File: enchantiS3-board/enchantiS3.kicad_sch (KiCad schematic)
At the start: 71 parts, among them J1 USB_C_Receptacle_USB2.0, Q1 BSS138, Q2 BSS138, Q3 BSS138, SW1 B3U-1000P, SW2 B3U-1000P, U1 USBLC6-2P6, U2 MCP73871, U3 NCP167AMX330TBG, U4 NCP167AMX180TBG

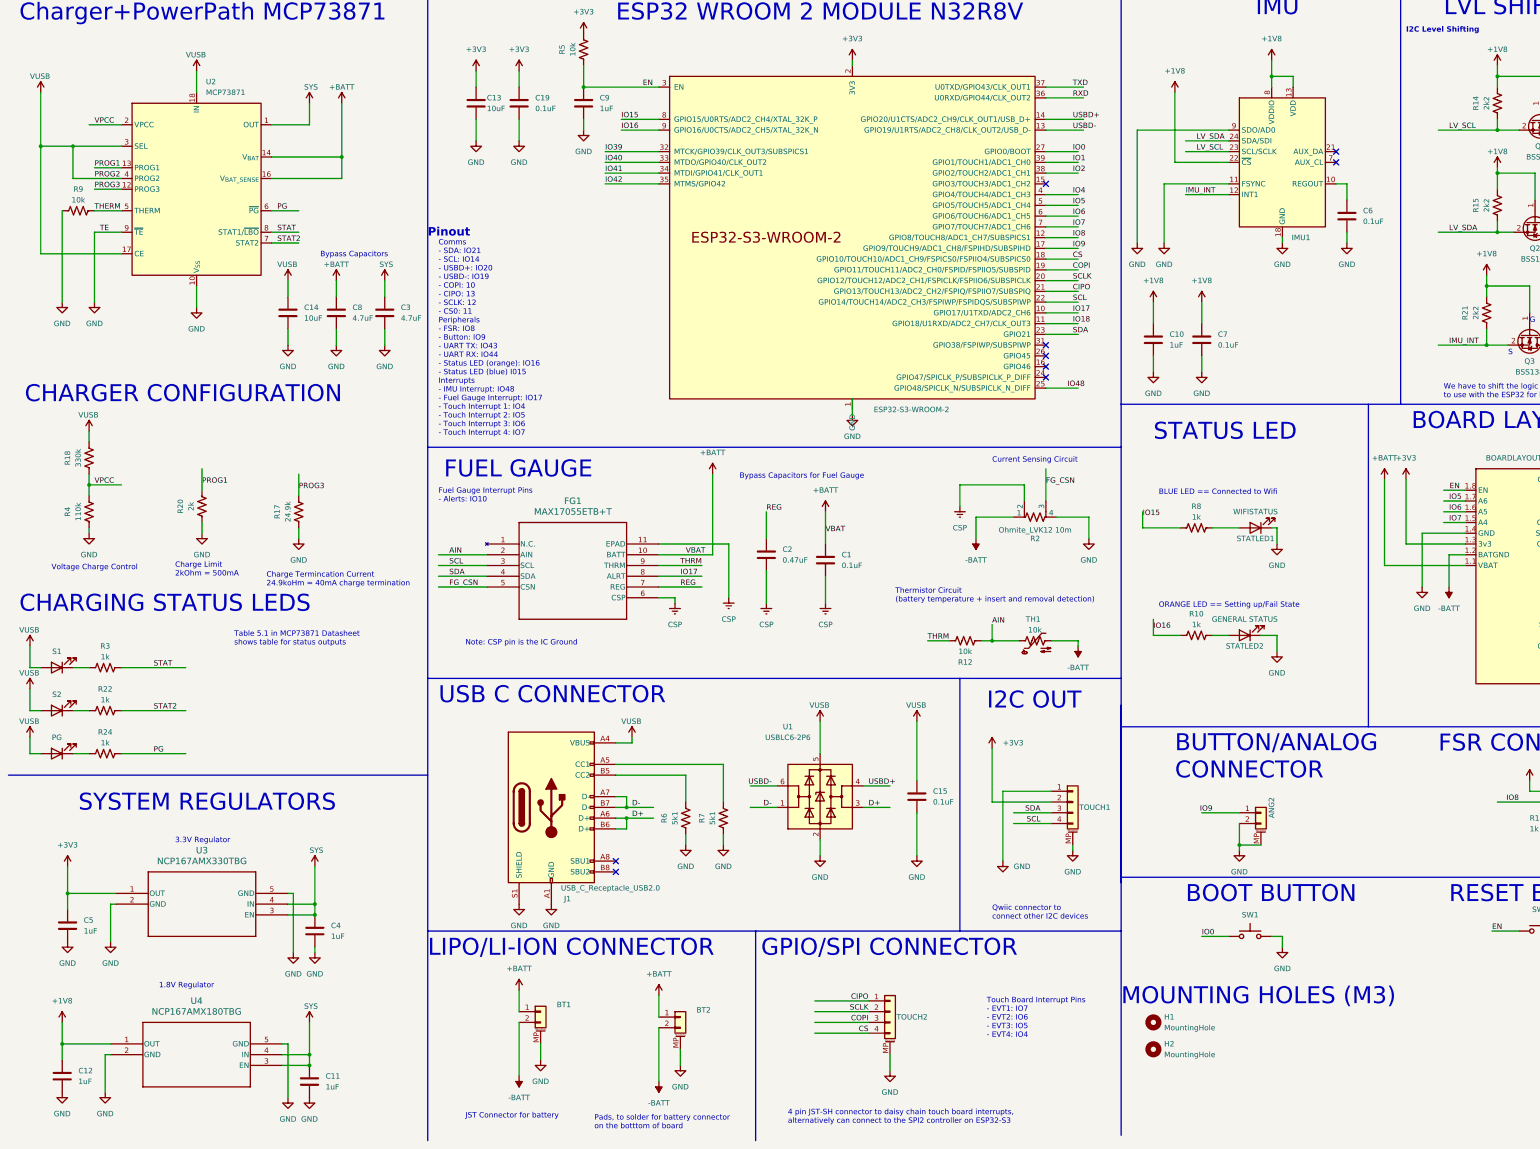
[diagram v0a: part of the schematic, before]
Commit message: added revision 3 board design
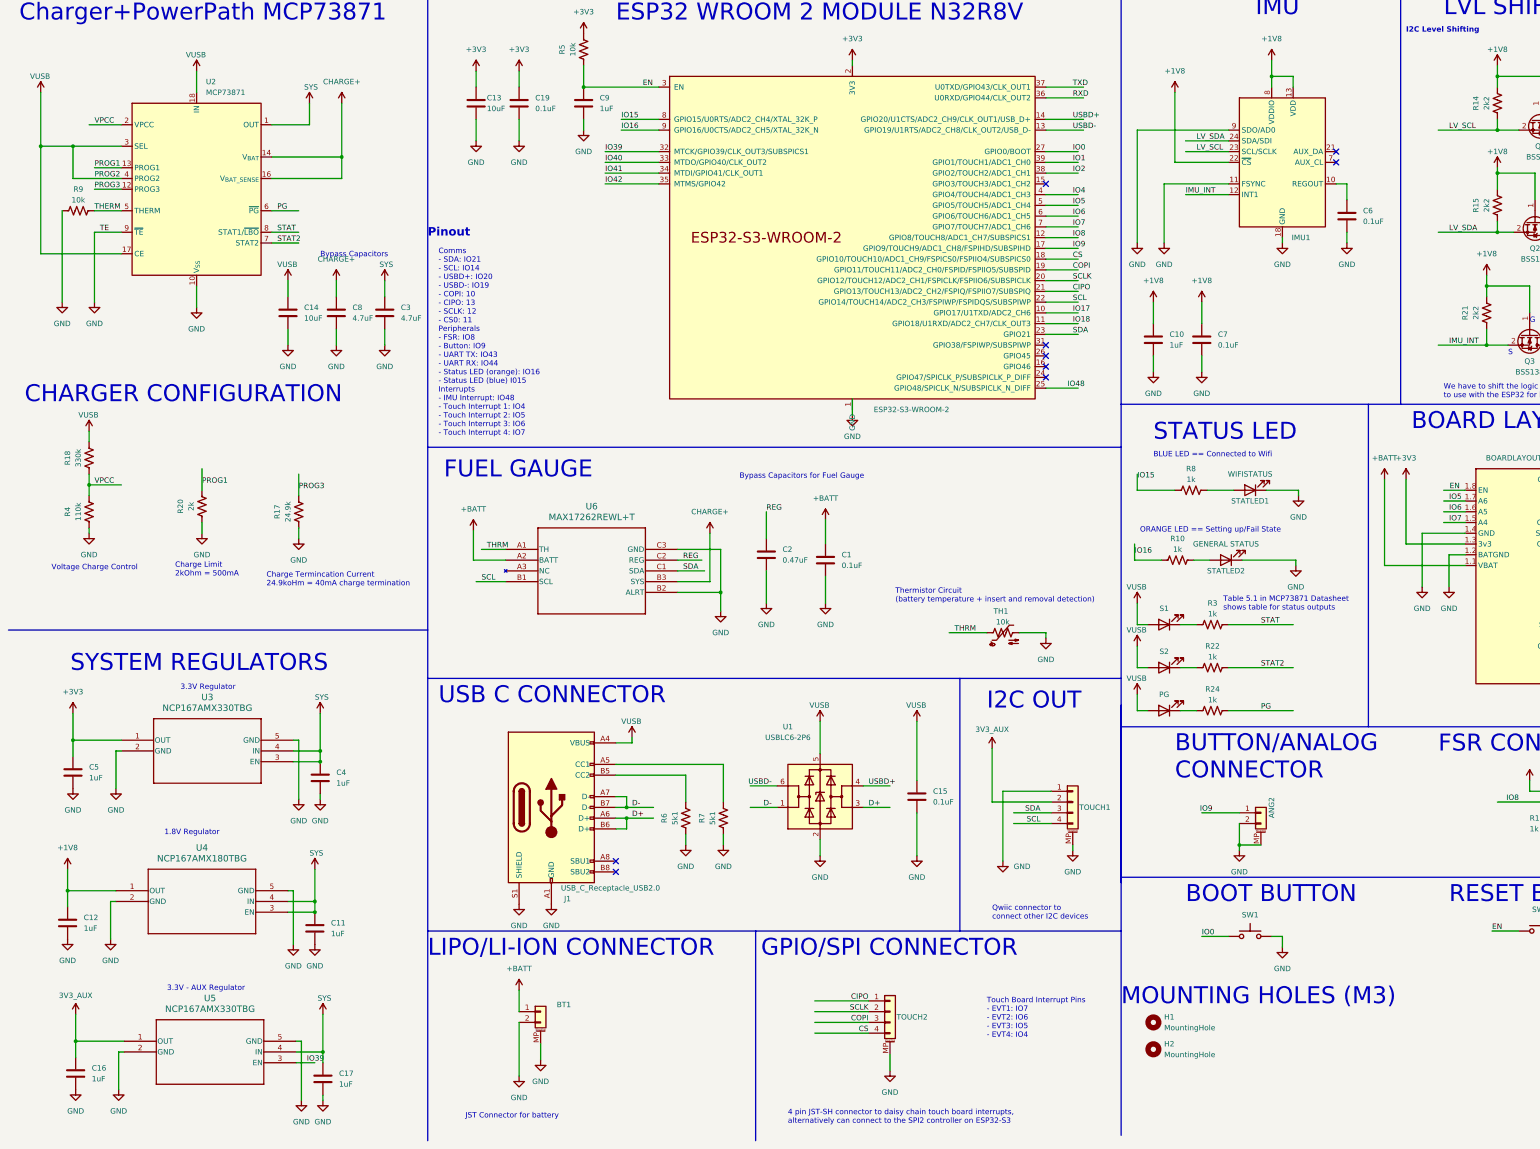
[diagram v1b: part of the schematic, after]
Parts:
- removed BT2: JST-PH-1x02-2.000mm, Connector_JST:JST_PH_S2B-PH-SM4-TB_1x02-1MP_P2.00mm_Horizontal, symbol Connector_Generic_MountingPin:Conn_01x02_MountingPin
- removed FG1: MAX17055ETB+T, max17055-footprints:21-100013A_T102A2&plus_1C_MXM, symbol max17055-symbol:MAX17055ETB+T
- removed R12: 10k, Resistor_SMD:R_0402_1005Metric, symbol Device:R_US
- removed R2: Ohmite_LVK12 10m, ul_LVK12R010CER-footprints:LVK12_OHM-L, symbol Device:R_Shunt_US
- added C16, C17: 1uF, Capacitor_SMD:C_0402_1005Metric, symbol Device:C
- added SYS4: SYS, symbol power-symbols:VSYS
- added U5: NCP167AMX330TBG, XDFN4_1X1_711AJ_ONS, symbol NCP167AMX330TBG:NCP167AMX330TBG
- added U6: MAX17262REWL+T, max17262-footprints:21-100221A_W91G1&plus_3_MXM, symbol max17262:MAX17262REWL+T
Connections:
- net -BATT is gone; now on net GND: BOARDLAYOUT1.1.2 (BATGND), BT1.2 (Pin_2), TH1.2
- net AIN is gone; now on net THRM: TH1.1
- net CSP is gone; now on net GND: C1.2, C2.2
- net +3V3: no longer TOUCH1.2 (Pin_2)
- net +BATT: now also U6.A2 (BATT); no longer C8.1, U2.14 (V_{BAT}), U2.15 (V_{BAT}), U2.16 (V_{BAT_SENSE})
- net GND: now also C16.2, C17.2, U5.2 (GND), U5.5 (GND), U6.B2 (ALRT), U6.C3 (GND)
- net IO39: now also U5.3 (EN)
- net REG: now also U6.C2 (REG)
- net SCL: now also U6.B1 (SCL)
- net SDA: now also U6.C1 (SDA)
- net SYS: now also C17.1, SYS4.1 (SYS), U5.4 (IN)
- net THRM: now also U6.A1 (TH)
- new net 3V3_AUX: C16.1, TOUCH1.2 (Pin_2), U5.1 (OUT)
- new net CHRG+: C8.1, U2.14 (V_{BAT}), U2.15 (V_{BAT}), U2.16 (V_{BAT_SENSE}), U6.B3 (SYS)
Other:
- note added: "3.3V - AUX Regulator"
- note added: "Comms - SDA: IO21 - SCL: IO14 - USBD+: IO20 - USBD-: IO19 - COPI: 10 - CIPO: 13 - SCLK: 12 - CS0: 11 Peripherals - FSR: IO8 - Button: IO9 - UART TX: IO43 - UART RX: IO44 - Status LED (orange): IO16 - Status LED (blue) I015 Interrupts - IMU Interrupt: IO48 - Touch Interrupt 1: IO4 - Touch Interrupt 2: IO5 - Touch Interrupt 3: IO6 - Touch Interrupt 4: IO7"
- note removed: "CHARGING STATUS LEDS"
- note removed: "Comms - SDA: IO21 - SCL: IO14 - USBD+: IO20 - USBD-: IO19 - COPI: 10 - CIPO: 13 - SCLK: 12 - CS0: 11 Peripherals - FSR: IO8 - Button: IO9 - UART TX: IO43 - UART RX: IO44 - Status LED (orange): IO16 - Status LED (blue) I015 Interrupts - IMU Interrupt: IO48 - Fuel Gauge Interrupt: IO17 - Touch Interrupt 1: IO4 - Touch Interrupt 2: IO5 - Touch Interrupt 3: IO6 - Touch Interrupt 4: IO7"
- note removed: "Current Sensing Circuit"
- note removed: "Fuel Gauge Interrupt Pins - Alerts: IO10"
- note removed: "Note: CSP pin is the IC Ground"
- note removed: "Pads, to solder for battery connector on the botttom of board"
- moved on the sheet: C11, C12, C4, C5, R10, R22, R24, R3, R8, STATLED1, STATLED2, TH1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

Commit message: fix BOM for revision 3 of the board
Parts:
- C13, C14: Mfg Part # CL10A105KO8NNNC -> CL10A106KQ8NNNC
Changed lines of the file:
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@@
       (effects (font (size 1.27 1.27)) hide)
     )
-    (property "Mfg Part #" "CL10A105KO8NNNC" (at 77.47 88.9 0)
+    (property "Mfg Part #" "CL10A106KQ8NNNC" (at 77.47 88.9 0)
       (effects (font (size 1.27 1.27)) hide)
     )
@@
       (effects (font (size 1.27 1.27)) hide)
     )
-    (property "Mfg Part #" "CL10A105KO8NNNC" (at 121.92 39.37 0)
-      (effects (font (size 1.27 1.27)) hide)
-    )
+    (property "Mfg Part #" "CL10A106KQ8NNNC" (at 121.92 39.37 0)
+      (effects (font (size 1.27 1.27)) hide)
+    )
